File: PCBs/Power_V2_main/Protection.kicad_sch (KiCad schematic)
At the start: 20 parts, among them J1 Conn_01x02, J12 Conn_01x02, J18 YK4420203000G, J2 Conn_01x02, J3 Conn_01x02, Q4 NTD25P03LT4G, U4 178.6164.0001, U5 TVS3300DRV, U9 AMS1117-3.3

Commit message: shortened main board and secondary
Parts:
- D1: footprint IPRL_footprints:SODFL1608X70N -> iprl_footprints:SODFL1608X70N
- D4: footprint IPRL_footprints:DIOM8059X265N -> iprl_footprints:DIOM8059X265N
- J18: footprint IPRL_footprints:RHDR2W120P0X950_1X2_2050X1430X1790P -> iprl_footprints:RHDR2W120P0X950_1X2_2050X1430X1790P
- Q4: footprint IPRL_footprints:MJD45H11T4G -> iprl_footprints:MJD45H11T4G
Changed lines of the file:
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@@
 			)
 		)
-		(property "Footprint" "IPRL_footprints:SODFL1608X70N"
+		(property "Footprint" "iprl_footprints:SODFL1608X70N"
 			(at 14.3 128.27 0)
 			(effects
@@
 			)
 		)
-		(property "Footprint" "IPRL_footprints:DIOM8059X265N"
+		(property "Footprint" "iprl_footprints:DIOM8059X265N"
 			(at 68.91 106.68 0)
 			(effects
@@
 			)
 		)
-		(property "Footprint" "IPRL_footprints:MJD45H11T4G"
+		(property "Footprint" "iprl_footprints:MJD45H11T4G"
 			(at 276.53 92.71 0)
 			(effects
@@
 			)
 		)
-		(property "Footprint" "IPRL_footprints:RHDR2W120P0X950_1X2_2050X1430X1790P"
+		(property "Footprint" "iprl_footprints:RHDR2W120P0X950_1X2_2050X1430X1790P"
 			(at 229.54 74.93 0)
 			(effects

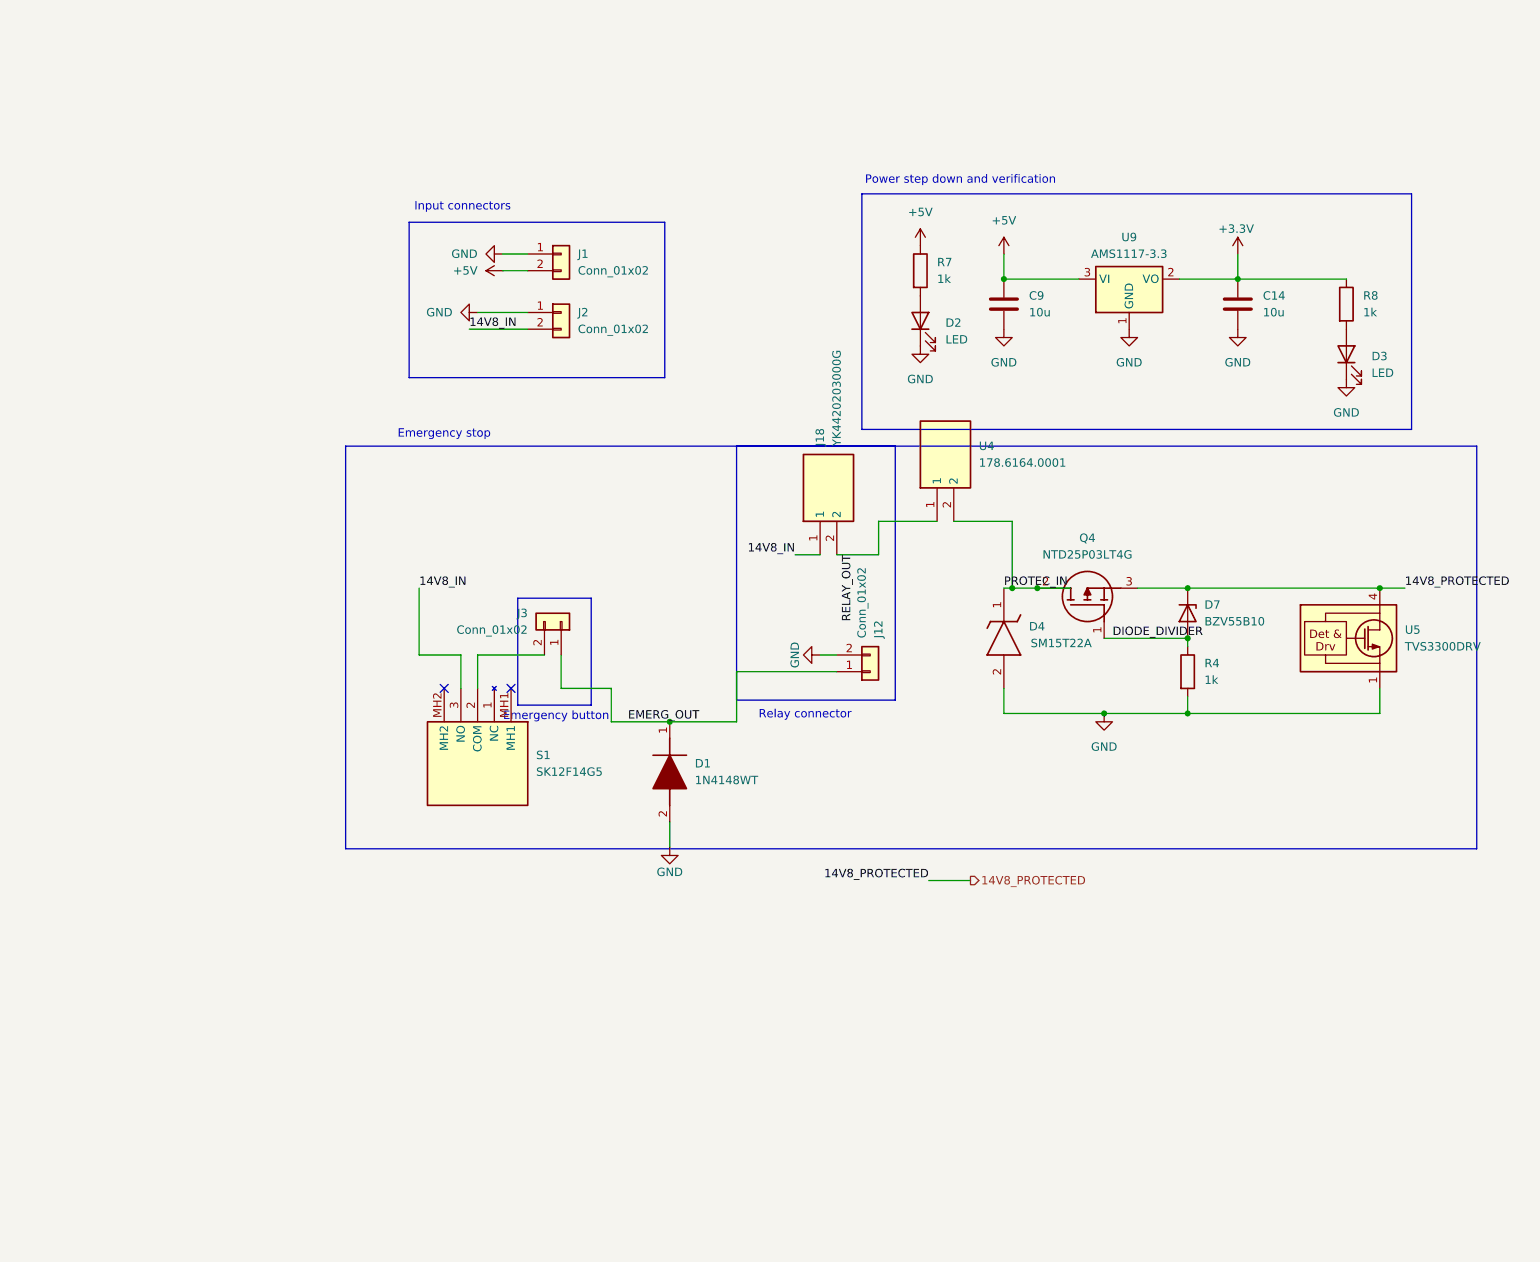
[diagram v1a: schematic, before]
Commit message: main schematic for power board main
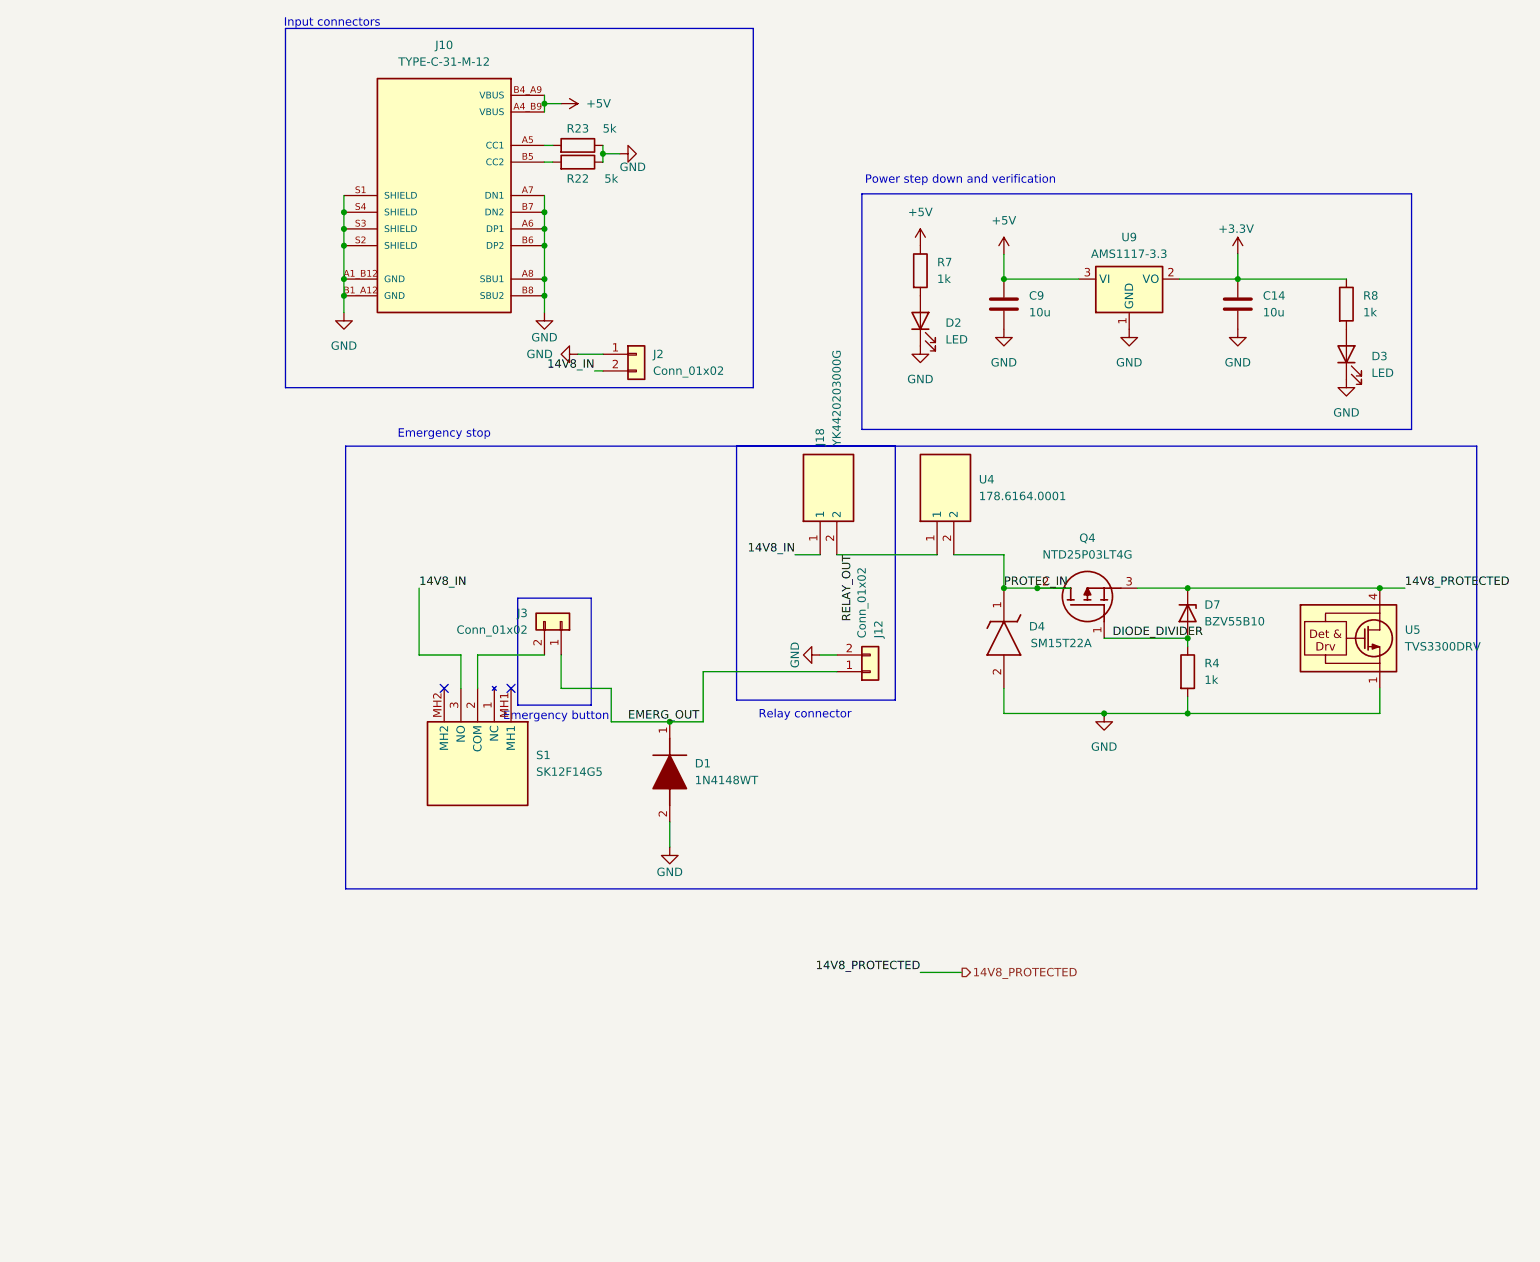
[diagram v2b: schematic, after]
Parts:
- removed J1: Conn_01x02, TerminalBlock:TerminalBlock_Altech_AK300-2_P5.00mm, symbol Connector_Generic:Conn_01x02
- added J10: TYPE-C-31-M-12, iprl_footprints:TYPE-C-31-M-12, symbol TYPE-C-31-M-12:TYPE-C-31-M-12
- added R22, R23: 5k, Resistor_SMD:R_0805_2012Metric, symbol Device:R
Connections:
- net +5V: now also J10.A4_B9 (VBUS), J10.B4_A9 (VBUS)
- net GND: now also J10.A1_B12 (GND), J10.A6 (DP1), J10.A7 (DN1), J10.A8 (SBU1), J10.B1_A12 (GND), J10.B6 (DP2), J10.B7 (DN2), J10.B8 (SBU2), J10.S1 (SHIELD), J10.S2 (SHIELD), J10.S3 (SHIELD), J10.S4 (SHIELD), R22.1, R23.1
- new net: J10.A5 (CC1), R23.2
- new net: J10.B5 (CC2), R22.2
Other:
- moved on the sheet: J2, U4

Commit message: a 5 hour binge of PCB layout on the main
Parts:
- removed D7: BZV55B10, Diode_SMD:D_MiniMELF, symbol Diode:BZV55B10
- removed Q4: NTD25P03LT4G, iprl_footprints:MJD45H11T4G, symbol NTD25P03LT4G:NTD25P03LT4G
- removed R4: 1k, Resistor_SMD:R_0805_2012Metric, symbol Device:R
- added R11: 63, Resistor_SMD:R_0805_2012Metric, symbol Device:R
- S1: footprint IPRL_footprints:SK12F14G5 -> iprl_footprints:SK12F14G5
- U4: footprint IPRL_footprints:178.6164.XXX1 -> iprl_footprints:178.6164.XXX1
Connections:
- net PROTEC_IN is gone; now on net 14V8_PROTECTED: D4.1 (K), U4.2
- net 14V8_IN: now also S1.2 (COM); no longer S1.3 (NO)
- net EMERG_OUT: now also J3.2 (Pin_2), R11.1; no longer J12.1 (Pin_1), J3.1 (Pin_1)
- net GND: now also J12.1 (Pin_1); no longer J12.2 (Pin_2)
- new net: J3.1 (Pin_1), S1.3 (NO)
- new net: J12.2 (Pin_2), R11.2
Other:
- note added: "5V power bank"
- note added: "5V step down"
- note added: "Power protection"
- note added: "Relay coil"
- note added: "XT90 Power input"
- note removed: "Emergency stop"
- note removed: "Input connectors"
- note removed: "Power step down and verification"
- note removed: "Relay connector"
- moved on the sheet: C14, C9, D1, D2, D3, D4, J10, J12, J18, J2, J3, R22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

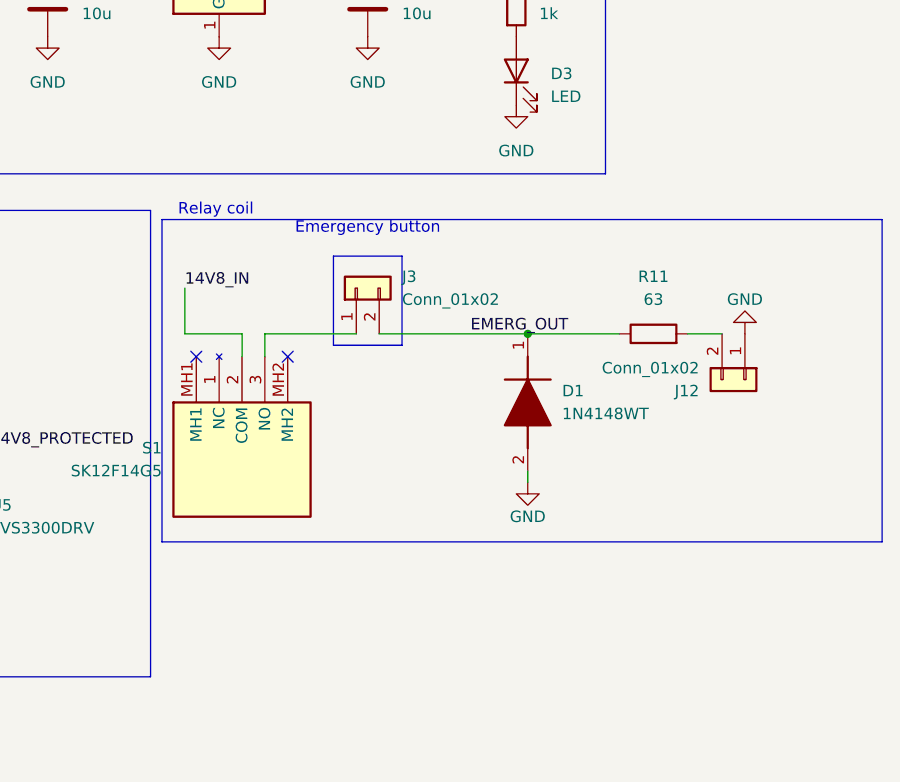
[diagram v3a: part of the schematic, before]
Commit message: added LED indicators to board and redid power distribution in PCIe
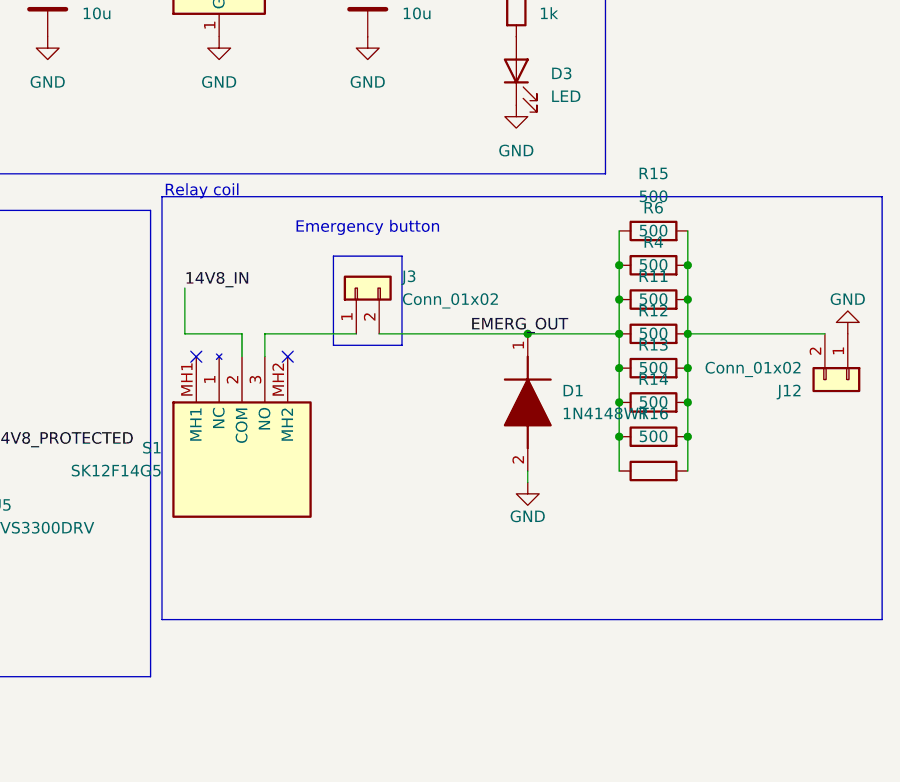
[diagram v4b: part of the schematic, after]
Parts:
- added R12, R13, R14, R15, R16, R4, R6: 500, Resistor_SMD:R_0805_2012Metric, symbol Device:R
- R11: value 63 -> 500
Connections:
- net EMERG_OUT: now also R12.1, R13.1, R14.1, R15.1, R16.1, R4.1, R6.1
- net at J12.2 (Pin_2), R11.2: now also R12.2, R13.2, R14.2, R15.2, R16.2, R4.2, R6.2
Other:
- moved on the sheet: J12

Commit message: Changes from meeting
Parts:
- D4: value SM15T22A -> SM15T22CA
- R22, R23: value 5k -> 5k1
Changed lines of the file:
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@@
 			)
 		)
-		(property "Value" "5k"
+		(property "Value" "5k1"
 			(at 110.236 55.88 90)
 			(effects
@@
 			)
 		)
-		(property "Value" "SM15T22A"
+		(property "Value" "SM15T22CA"
 			(at 106.934 134.112 90)
 			(effects
@@
 			)
 		)
-		(property "Value" "5k"
+		(property "Value" "5k1"
 			(at 110.49 63.5 90)
 			(effects

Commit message: follow up changes from meeting
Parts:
- removed R11, R12, R13, R14, R15, R16, R6: 500, Resistor_SMD:R_0805_2012Metric, symbol Device:R
- R4: value 500 -> 65; footprint Resistor_SMD:R_0805_2012Metric -> Resistor_THT:R_Axial_DIN0414_L11.9mm_D4.5mm_P15.24mm_Horizontal
